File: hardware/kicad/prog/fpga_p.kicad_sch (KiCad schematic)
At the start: 28 parts, among them J3 CONF P, U10 iCE40HX4K-TQ144, X1 25 MHz 3,3 V

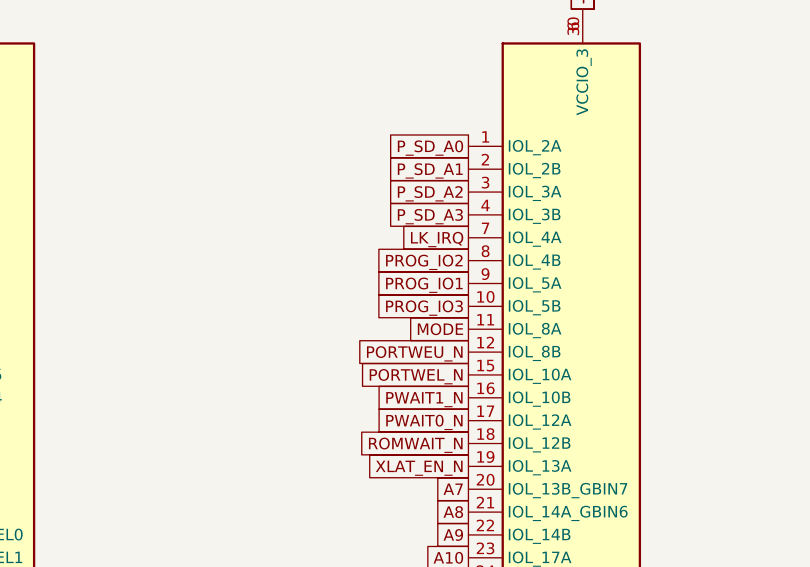
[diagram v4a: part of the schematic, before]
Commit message: Pico 2, microSD et bouton sur la carte PROG ; pistes d'alimentation larges
- La carte PROG est côté avant de la cartouche, composants vers l'avant :
  lecteur microSD et bouton accessibles. Le câble PROG-CHA porte
  désormais le bus de liaison C/SM ; connecteur au même endroit sur les
  deux cartes (x = 172 mm), prêt pour un connecteur carte à carte.
- Sous le Pico : ni piste ni via sur la face composants (pastilles de
  test nues sous le module).
- Classes de réseaux écrites dans le .kicad_pro : +5V et VSYS en 0,5 mm,
  +1V2 en 0,3 mm.
- Broches des FPGA réoptimisées ; contrôle Freerouting sans violation ;
  routage des deux cartes et vérification de timing en cours.

Co-Authored-By: Claude Opus 5.5 <noreply@anthropic.com>
Claude-Session: https://claude.ai/code/session_01WKfXP1YJ8otGxZ5dsY6Agh
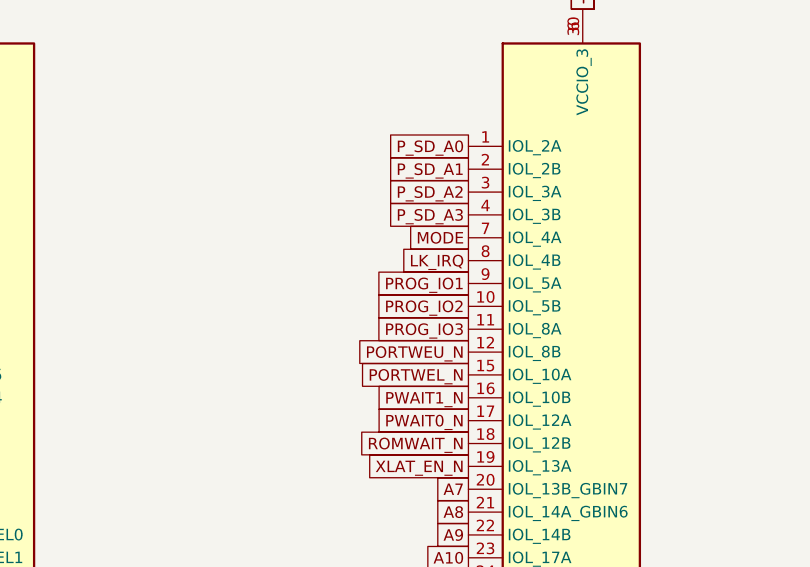
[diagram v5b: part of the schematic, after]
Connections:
- net LK_IRQ: now also U10.8 (IOL_4B); no longer U10.7 (IOL_4A)
- net MODE: now also U10.7 (IOL_4A); no longer U10.11 (IOL_8A)
- net PROG_IO2: now also U10.10 (IOL_5B); no longer U10.8 (IOL_4B)
- net PROG_IO3: now also U10.11 (IOL_8A); no longer U10.10 (IOL_5B)
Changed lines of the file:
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@@
     (instances
       (project "prog"
-        (path "/da9dbc37-1614-4aa0-819a-d60fb574ce37/8b94eec3-2392-48d5-ae46-266e4de8bcc3"
+        (path "/730f52e2-cd0f-4a48-866b-cc2c9ca510b4/14afbfe5-16f5-4bd8-9405-c6b4ead158a3"
           (reference "U10")
           (unit 1)))))
@@
     (instances
       (project "prog"
-        (path "/da9dbc37-1614-4aa0-819a-d60fb574ce37/8b94eec3-2392-48d5-ae46-266e4de8bcc3"
+        (path "/730f52e2-cd0f-4a48-866b-cc2c9ca510b4/14afbfe5-16f5-4bd8-9405-c6b4ead158a3"
           (reference "U10")
           (unit 2)))))
@@
     (instances
       (project "prog"
-        (path "/da9dbc37-1614-4aa0-819a-d60fb574ce37/8b94eec3-2392-48d5-ae46-266e4de8bcc3"
+        (path "/730f52e2-cd0f-4a48-866b-cc2c9ca510b4/14afbfe5-16f5-4bd8-9405-c6b4ead158a3"
           (reference "U10")
           (unit 3)))))
@@
     (instances
       (project "prog"
-        (path "/da9dbc37-1614-4aa0-819a-d60fb574ce37/8b94eec3-2392-48d5-ae46-266e4de8bcc3"
+        (path "/730f52e2-cd0f-4a48-866b-cc2c9ca510b4/14afbfe5-16f5-4bd8-9405-c6b4ead158a3"
           (reference "U10")
           (unit 4)))))
@@
         (font
           (size 1.27 1.27)) hide)))
-  (global_label "PROG_IO3"
+  (global_label "PROG_IO2"
     (shape passive)
     (at 259.08 71.12 180)
@@
         (font
           (size 1.27 1.27)) hide)))
-  (global_label "MODE"
+  (global_label "PROG_IO3"
     (shape passive)
     (at 259.08 73.66 180)
@@
         (font
           (size 1.27 1.27)) hide)))
-  (global_label "LK_IRQ"
+  (global_label "MODE"
     (shape passive)
     (at 259.08 63.5 180)
@@
         (font
           (size 1.27 1.27)) hide)))
-  (global_label "PROG_IO2"
+  (global_label "LK_IRQ"
     (shape passive)
     (at 259.08 66.04 180)
@@
     (instances
       (project "prog"
-        (path "/da9dbc37-1614-4aa0-819a-d60fb574ce37/8b94eec3-2392-48d5-ae46-266e4de8bcc3"
+        (path "/730f52e2-cd0f-4a48-866b-cc2c9ca510b4/14afbfe5-16f5-4bd8-9405-c6b4ead158a3"
           (reference "U10")
           (unit 5)))))
@@
     (instances
       (project "prog"
-        (path "/da9dbc37-1614-4aa0-819a-d60fb574ce37/8b94eec3-2392-48d5-ae46-266e4de8bcc3"
+        (path "/730f52e2-cd0f-4a48-866b-cc2c9ca510b4/14afbfe5-16f5-4bd8-9405-c6b4ead158a3"
           (reference "C19")
           (unit 1)))))
@@
     (instances
       (project "prog"
-        (path "/da9dbc37-1614-4aa0-819a-d60fb574ce37/8b94eec3-2392-48d5-ae46-266e4de8bcc3"
+        (path "/730f52e2-cd0f-4a48-866b-cc2c9ca510b4/14afbfe5-16f5-4bd8-9405-c6b4ead158a3"
           (reference "C20")
           (unit 1)))))
@@
     (instances
       (project "prog"
-        (path "/da9dbc37-1614-4aa0-819a-d60fb574ce37/8b94eec3-2392-48d5-ae46-266e4de8bcc3"
+        (path "/730f52e2-cd0f-4a48-866b-cc2c9ca510b4/14afbfe5-16f5-4bd8-9405-c6b4ead158a3"
           (reference "C21")
           (unit 1)))))
@@
     (instances
       (project "prog"
-        (path "/da9dbc37-1614-4aa0-819a-d60fb574ce37/8b94eec3-2392-48d5-ae46-266e4de8bcc3"
+        (path "/730f52e2-cd0f-4a48-866b-cc2c9ca510b4/14afbfe5-16f5-4bd8-9405-c6b4ead158a3"
           (reference "C22")
           (unit 1)))))
@@
     (instances
       (project "prog"
-        (path "/da9dbc37-1614-4aa0-819a-d60fb574ce37/8b94eec3-2392-48d5-ae46-266e4de8bcc3"
+        (path "/730f52e2-cd0f-4a48-866b-cc2c9ca510b4/14afbfe5-16f5-4bd8-9405-c6b4ead158a3"
           (reference "C23")
           (unit 1)))))
@@
     (instances
       (project "prog"
-        (path "/da9dbc37-1614-4aa0-819a-d60fb574ce37/8b94eec3-2392-48d5-ae46-266e4de8bcc3"
+        (path "/730f52e2-cd0f-4a48-866b-cc2c9ca510b4/14afbfe5-16f5-4bd8-9405-c6b4ead158a3"
           (reference "C24")
           (unit 1)))))
@@
     (instances
       (project "prog"
-        (path "/da9dbc37-1614-4aa0-819a-d60fb574ce37/8b94eec3-2392-48d5-ae46-266e4de8bcc3"
+        (path "/730f52e2-cd0f-4a48-866b-cc2c9ca510b4/14afbfe5-16f5-4bd8-9405-c6b4ead158a3"
           (reference "C25")
           (unit 1)))))
@@
     (instances
       (project "prog"
-        (path "/da9dbc37-1614-4aa0-819a-d60fb574ce37/8b94eec3-2392-48d5-ae46-266e4de8bcc3"
+        (path "/730f52e2-cd0f-4a48-866b-cc2c9ca510b4/14afbfe5-16f5-4bd8-9405-c6b4ead158a3"
           (reference "C26")
           (unit 1)))))
@@
     (instances
       (project "prog"
-        (path "/da9dbc37-1614-4aa0-819a-d60fb574ce37/8b94eec3-2392-48d5-ae46-266e4de8bcc3"
+        (path "/730f52e2-cd0f-4a48-866b-cc2c9ca510b4/14afbfe5-16f5-4bd8-9405-c6b4ead158a3"
           (reference "C27")
           (unit 1)))))
@@
     (instances
       (project "prog"
-        (path "/da9dbc37-1614-4aa0-819a-d60fb574ce37/8b94eec3-2392-48d5-ae46-266e4de8bcc3"
+        (path "/730f52e2-cd0f-4a48-866b-cc2c9ca510b4/14afbfe5-16f5-4bd8-9405-c6b4ead158a3"
           (reference "C28")
           (unit 1)))))
@@
     (instances
       (project "prog"
-        (path "/da9dbc37-1614-4aa0-819a-d60fb574ce37/8b94eec3-2392-48d5-ae46-266e4de8bcc3"
+        (path "/730f52e2-cd0f-4a48-866b-cc2c9ca510b4/14afbfe5-16f5-4bd8-9405-c6b4ead158a3"
           (reference "C29")
           (unit 1)))))
@@
     (instances
       (project "prog"
-        (path "/da9dbc37-1614-4aa0-819a-d60fb574ce37/8b94eec3-2392-48d5-ae46-266e4de8bcc3"
+        (path "/730f52e2-cd0f-4a48-866b-cc2c9ca510b4/14afbfe5-16f5-4bd8-9405-c6b4ead158a3"
           (reference "C30")
           (unit 1)))))
@@
     (instances
       (project "prog"
-        (path "/da9dbc37-1614-4aa0-819a-d60fb574ce37/8b94eec3-2392-48d5-ae46-266e4de8bcc3"
+        (path "/730f52e2-cd0f-4a48-866b-cc2c9ca510b4/14afbfe5-16f5-4bd8-9405-c6b4ead158a3"
           (reference "C31")
           (unit 1)))))
@@
     (instances
       (project "prog"
-        (path "/da9dbc37-1614-4aa0-819a-d60fb574ce37/8b94eec3-2392-48d5-ae46-266e4de8bcc3"
+        (path "/730f52e2-cd0f-4a48-866b-cc2c9ca510b4/14afbfe5-16f5-4bd8-9405-c6b4ead158a3"
           (reference "C32")
           (unit 1)))))
@@
     (instances
       (project "prog"
-        (path "/da9dbc37-1614-4aa0-819a-d60fb574ce37/8b94eec3-2392-48d5-ae46-266e4de8bcc3"
+        (path "/730f52e2-cd0f-4a48-866b-cc2c9ca510b4/14afbfe5-16f5-4bd8-9405-c6b4ead158a3"
           (reference "C33")
           (unit 1)))))
@@
     (instances
       (project "prog"
-        (path "/da9dbc37-1614-4aa0-819a-d60fb574ce37/8b94eec3-2392-48d5-ae46-266e4de8bcc3"
+        (path "/730f52e2-cd0f-4a48-866b-cc2c9ca510b4/14afbfe5-16f5-4bd8-9405-c6b4ead158a3"
           (reference "R10")
           (unit 1)))))
@@
     (instances
       (project "prog"
-        (path "/da9dbc37-1614-4aa0-819a-d60fb574ce37/8b94eec3-2392-48d5-ae46-266e4de8bcc3"
+        (path "/730f52e2-cd0f-4a48-866b-cc2c9ca510b4/14afbfe5-16f5-4bd8-9405-c6b4ead158a3"
           (reference "C34")
           (unit 1)))))
@@
     (instances
       (project "prog"
-        (path "/da9dbc37-1614-4aa0-819a-d60fb574ce37/8b94eec3-2392-48d5-ae46-266e4de8bcc3"
+        (path "/730f52e2-cd0f-4a48-866b-cc2c9ca510b4/14afbfe5-16f5-4bd8-9405-c6b4ead158a3"
           (reference "C35")
           (unit 1)))))
@@
     (instances
       (project "prog"
-        (path "/da9dbc37-1614-4aa0-819a-d60fb574ce37/8b94eec3-2392-48d5-ae46-266e4de8bcc3"
+        (path "/730f52e2-cd0f-4a48-866b-cc2c9ca510b4/14afbfe5-16f5-4bd8-9405-c6b4ead158a3"
           (reference "R11")
           (unit 1)))))
@@
     (instances
       (project "prog"
-        (path "/da9dbc37-1614-4aa0-819a-d60fb574ce37/8b94eec3-2392-48d5-ae46-266e4de8bcc3"
+        (path "/730f52e2-cd0f-4a48-866b-cc2c9ca510b4/14afbfe5-16f5-4bd8-9405-c6b4ead158a3"
           (reference "C36")
           (unit 1)))))
@@
     (instances
       (project "prog"
-        (path "/da9dbc37-1614-4aa0-819a-d60fb574ce37/8b94eec3-2392-48d5-ae46-266e4de8bcc3"
+        (path "/730f52e2-cd0f-4a48-866b-cc2c9ca510b4/14afbfe5-16f5-4bd8-9405-c6b4ead158a3"
           (reference "C37")
           (unit 1)))))
@@
     (instances
       (project "prog"
-        (path "/da9dbc37-1614-4aa0-819a-d60fb574ce37/8b94eec3-2392-48d5-ae46-266e4de8bcc3"
+        (path "/730f52e2-cd0f-4a48-866b-cc2c9ca510b4/14afbfe5-16f5-4bd8-9405-c6b4ead158a3"
           (reference "R12")
           (unit 1)))))
@@
     (instances
       (project "prog"
-        (path "/da9dbc37-1614-4aa0-819a-d60fb574ce37/8b94eec3-2392-48d5-ae46-266e4de8bcc3"
+        (path "/730f52e2-cd0f-4a48-866b-cc2c9ca510b4/14afbfe5-16f5-4bd8-9405-c6b4ead158a3"
           (reference "J3")
           (unit 1)))))
@@
     (instances
       (project "prog"
-        (path "/da9dbc37-1614-4aa0-819a-d60fb574ce37/8b94eec3-2392-48d5-ae46-266e4de8bcc3"
+        (path "/730f52e2-cd0f-4a48-866b-cc2c9ca510b4/14afbfe5-16f5-4bd8-9405-c6b4ead158a3"
           (reference "X1")
           (unit 1)))))
@@
     (instances
       (project "prog"
-        (path "/da9dbc37-1614-4aa0-819a-d60fb574ce37/8b94eec3-2392-48d5-ae46-266e4de8bcc3"
+        (path "/730f52e2-cd0f-4a48-866b-cc2c9ca510b4/14afbfe5-16f5-4bd8-9405-c6b4ead158a3"
           (reference "C38")
           (unit 1)))))
@@
     (instances
       (project "prog"
-        (path "/da9dbc37-1614-4aa0-819a-d60fb574ce37/8b94eec3-2392-48d5-ae46-266e4de8bcc3"
+        (path "/730f52e2-cd0f-4a48-866b-cc2c9ca510b4/14afbfe5-16f5-4bd8-9405-c6b4ead158a3"
           (reference "R13")
           (unit 1)))))
@@
     (instances
       (project "prog"
-        (path "/da9dbc37-1614-4aa0-819a-d60fb574ce37/8b94eec3-2392-48d5-ae46-266e4de8bcc3"
+        (path "/730f52e2-cd0f-4a48-866b-cc2c9ca510b4/14afbfe5-16f5-4bd8-9405-c6b4ead158a3"
           (reference "D1")
           (unit 1)))))

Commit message: Régulateur 3,3 V à découpage, horloge SDRAM adaptée côté FPGA, U8 en 74AHCT125
- AP63203 (TSOT-23-6, sortie fixe 3,3 V, ~90 %) à la place de
  l'AMS1117 : ~0,15 W de pertes au lieu de ~0,75 W et moins de courant
  tiré sur le 5 V de la console ; L 4,7 µH, Cin 10 µF, Cout 2 x 22 µF.
- Résistance série de 33 ohms de l'horloge SDRAM déclarée avec le FPGA :
  placée à 2,7 mm de sa broche (au lieu de ~30 mm, côté SDRAM).
- CHA : U8 (16244 pour 2 canaux) remplacé par un 74AHCT125.
Cartes replacées, contrôle Freerouting sans violation ; routage des
deux cartes et vérification de timing en cours.

Co-Authored-By: Claude Opus 5.5 <noreply@anthropic.com>
Claude-Session: https://claude.ai/code/session_01WKfXP1YJ8otGxZ5dsY6Agh
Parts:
- removed C19, C20: 100n, Capacitor_SMD:C_0603_1608Metric, symbol Device:C
- added C39, C40: 100n, Capacitor_SMD:C_0603_1608Metric, symbol Device:C
- added R14: 470, Resistor_SMD:R_0603_1608Metric, symbol Device:R
- C23, C33, C34: value 10u -> 100n; footprint Capacitor_SMD:C_0805_2012Metric -> Capacitor_SMD:C_0603_1608Metric
- C25, C35, C38: value 100n -> 10u; footprint Capacitor_SMD:C_0603_1608Metric -> Capacitor_SMD:C_0805_2012Metric
- R13: value 470 -> 33
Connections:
- net +1V2: now also C24.1, C25.1
- net +3V3: now also C34.1, C35.1, C40.1; no longer C24.1, C25.1, C38.1
- net GND: now also C39.2, C40.2
- net P_LED: now also U10.81 (IOR_117), R14.1; no longer R13.1, U10.87 (IOR_136)
- net P_LED_K: now also R14.2; no longer R13.2
- net P_SD_CLK: now also R13.1, U10.94 (IOR_141_GBIN2); no longer U10.97 (IOR_147)
- net P_VCCPLL0: now also C36.1, C37.1; no longer C34.1, C35.1
- net P_VCCPLL1: now also C38.1, C39.1; no longer C36.1, C37.1
- new net P_SD_CLK_R: R13.2
